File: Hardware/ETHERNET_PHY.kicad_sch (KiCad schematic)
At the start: 20 parts, among them J15 RJ45_Hanrun_HR911105A_Horizon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, U45 JL1111-N032I

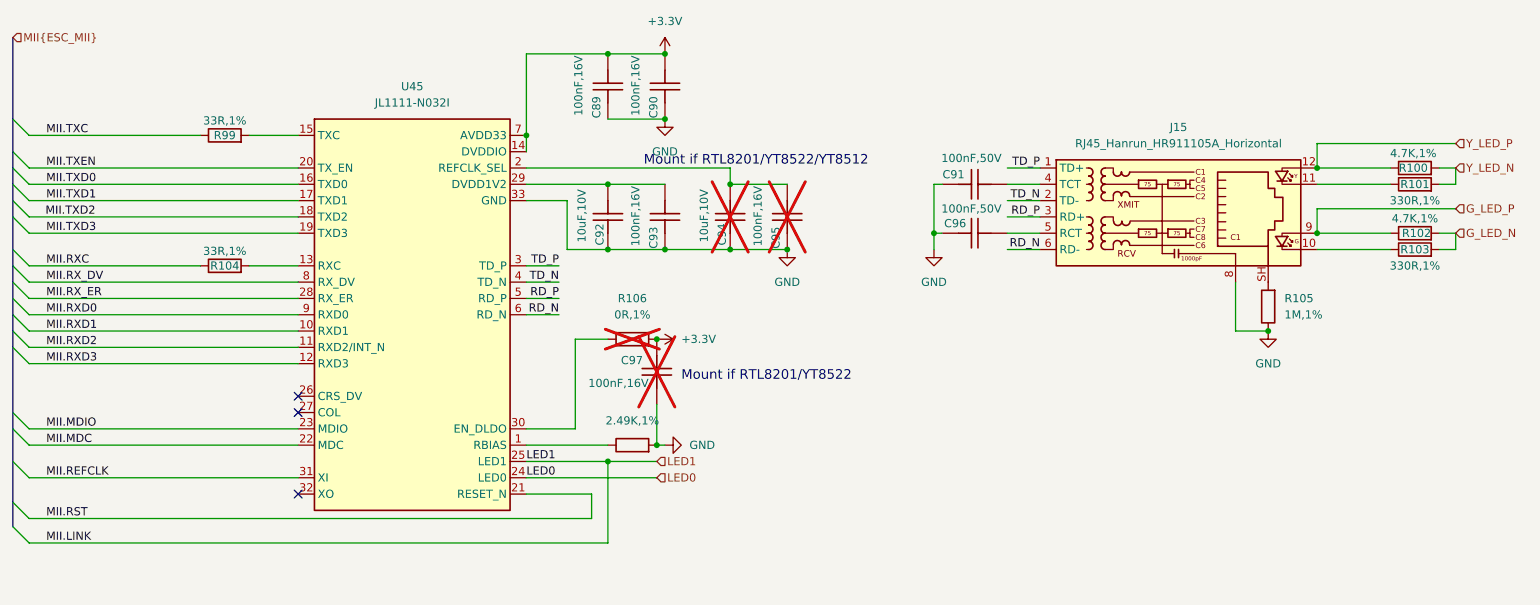
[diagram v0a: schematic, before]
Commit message: PCB：网口替换为HR911205C
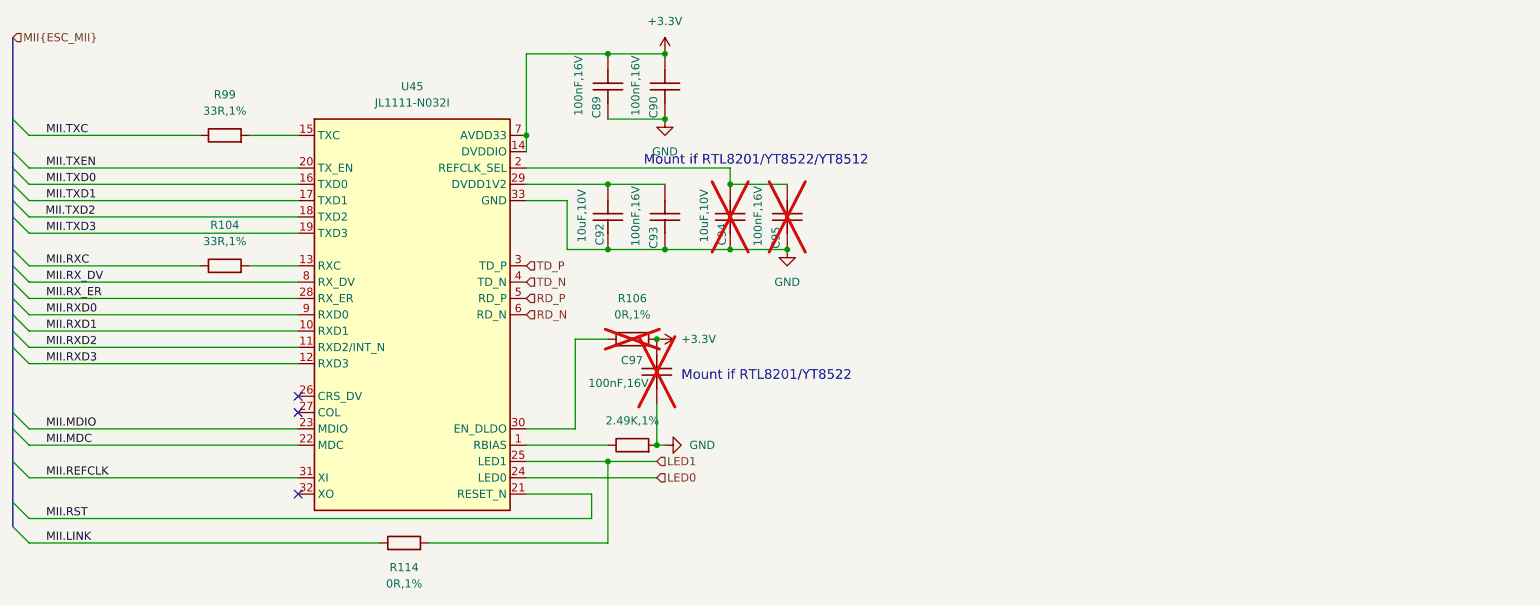
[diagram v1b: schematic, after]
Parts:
- removed C91, C96: 100nF,50V, Capacitor_SMD:C_0603_1608Metric, symbol HPM6280Foc:CC0603KRX7R9BB104
- removed J15: RJ45_Hanrun_HR911105A_Horizontal, Connector_RJ:RJ45_Hanrun_HR911105A_Horizontal, symbol Connector:RJ45_Hanrun_HR911105A_Horizontal
- removed R100, R102: 4.7K,1%, Resistor_SMD:R_0402_1005Metric, symbol HPM6280Foc:0402WGF4701TCE
- removed R101, R103: 330R,1%, Resistor_SMD:R_0402_1005Metric, symbol HPM6280Foc:0402WGF3300TCE
- removed R105: 1M,1%, Resistor_SMD:R_0805_2012Metric, symbol HPM6280Foc:0805W8F1004T5E
- added R114: 0R,1%, Resistor_SMD:R_0201_0603Metric, symbol HPM6280Foc:0201WMF0000TEE
- R104, R99: footprint Resistor_SMD:R_0402_1005Metric -> Resistor_SMD:R_0201_0603Metric; symbol HPM6280Foc:0402WGF330JTCE -> HPM6280Foc:RC0201FR-0733RL; 立创编号 C25105 -> C295794
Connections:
- net LED1: now also R114.2
- new net MII.LINK: R114.1
